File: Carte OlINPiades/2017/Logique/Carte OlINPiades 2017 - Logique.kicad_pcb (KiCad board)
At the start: 2 copper layers, 258 parts

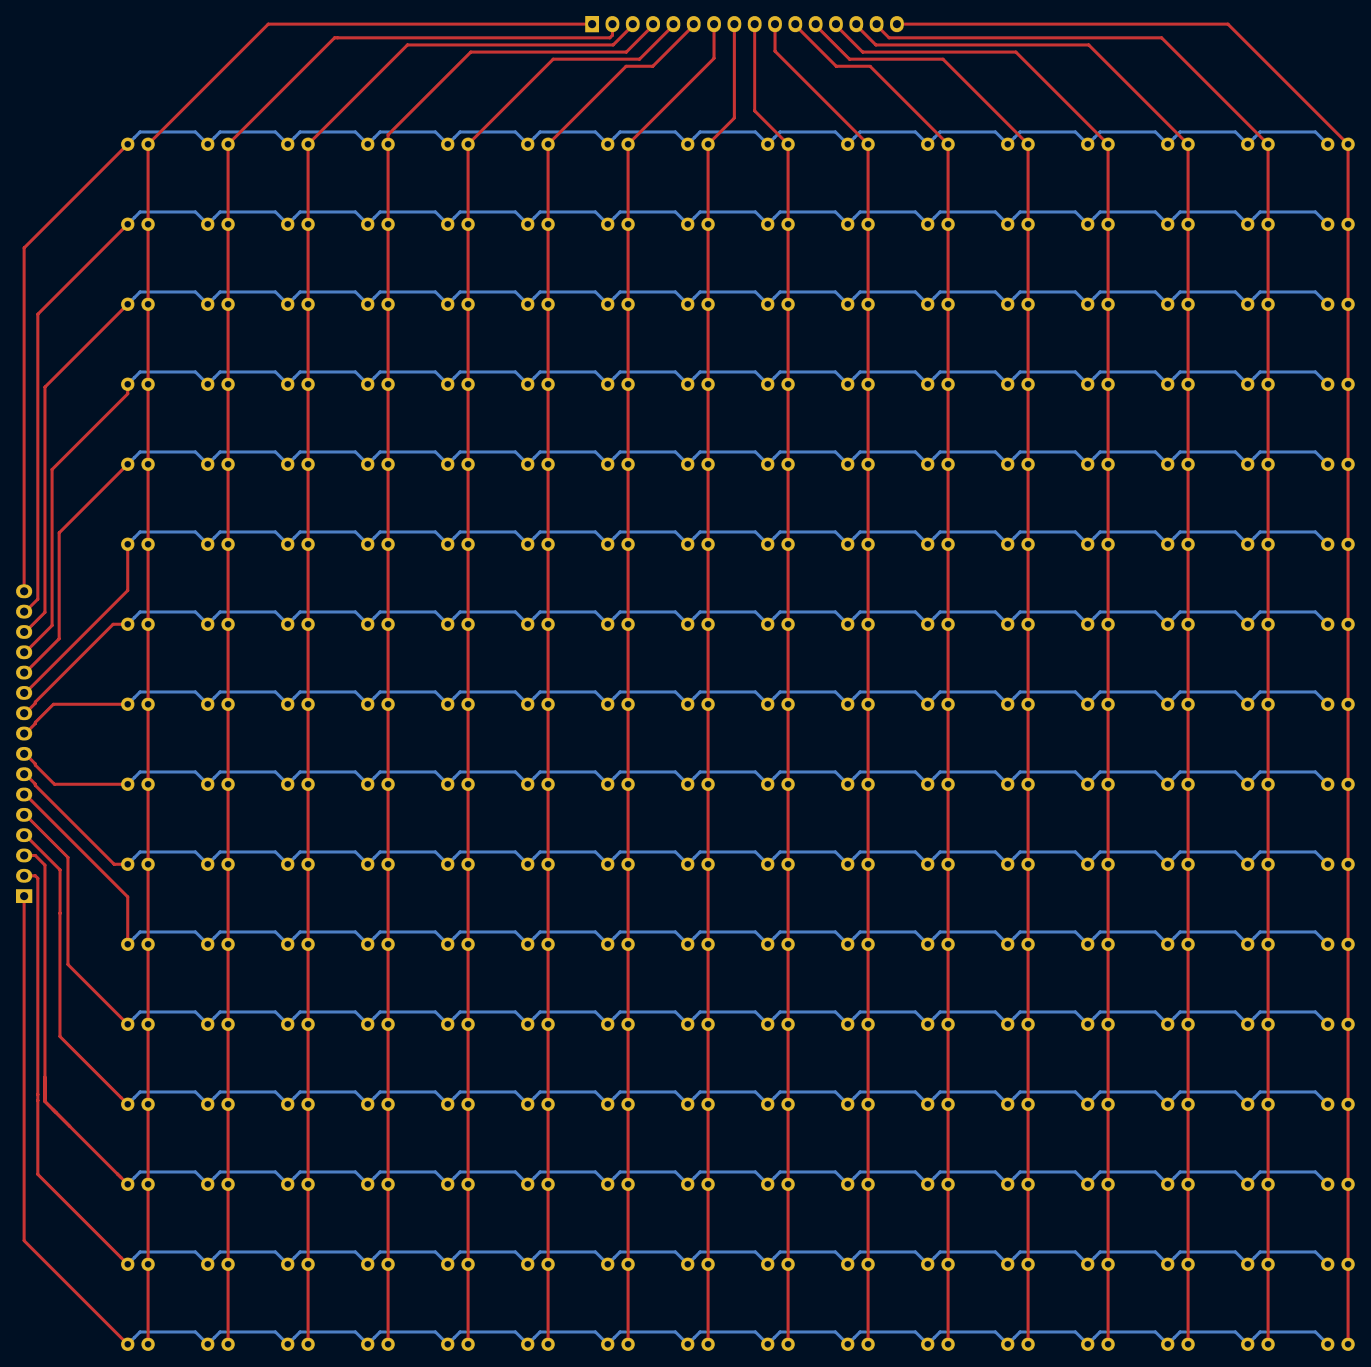
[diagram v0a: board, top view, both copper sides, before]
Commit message: Routage carte Logique fini, à vérifier
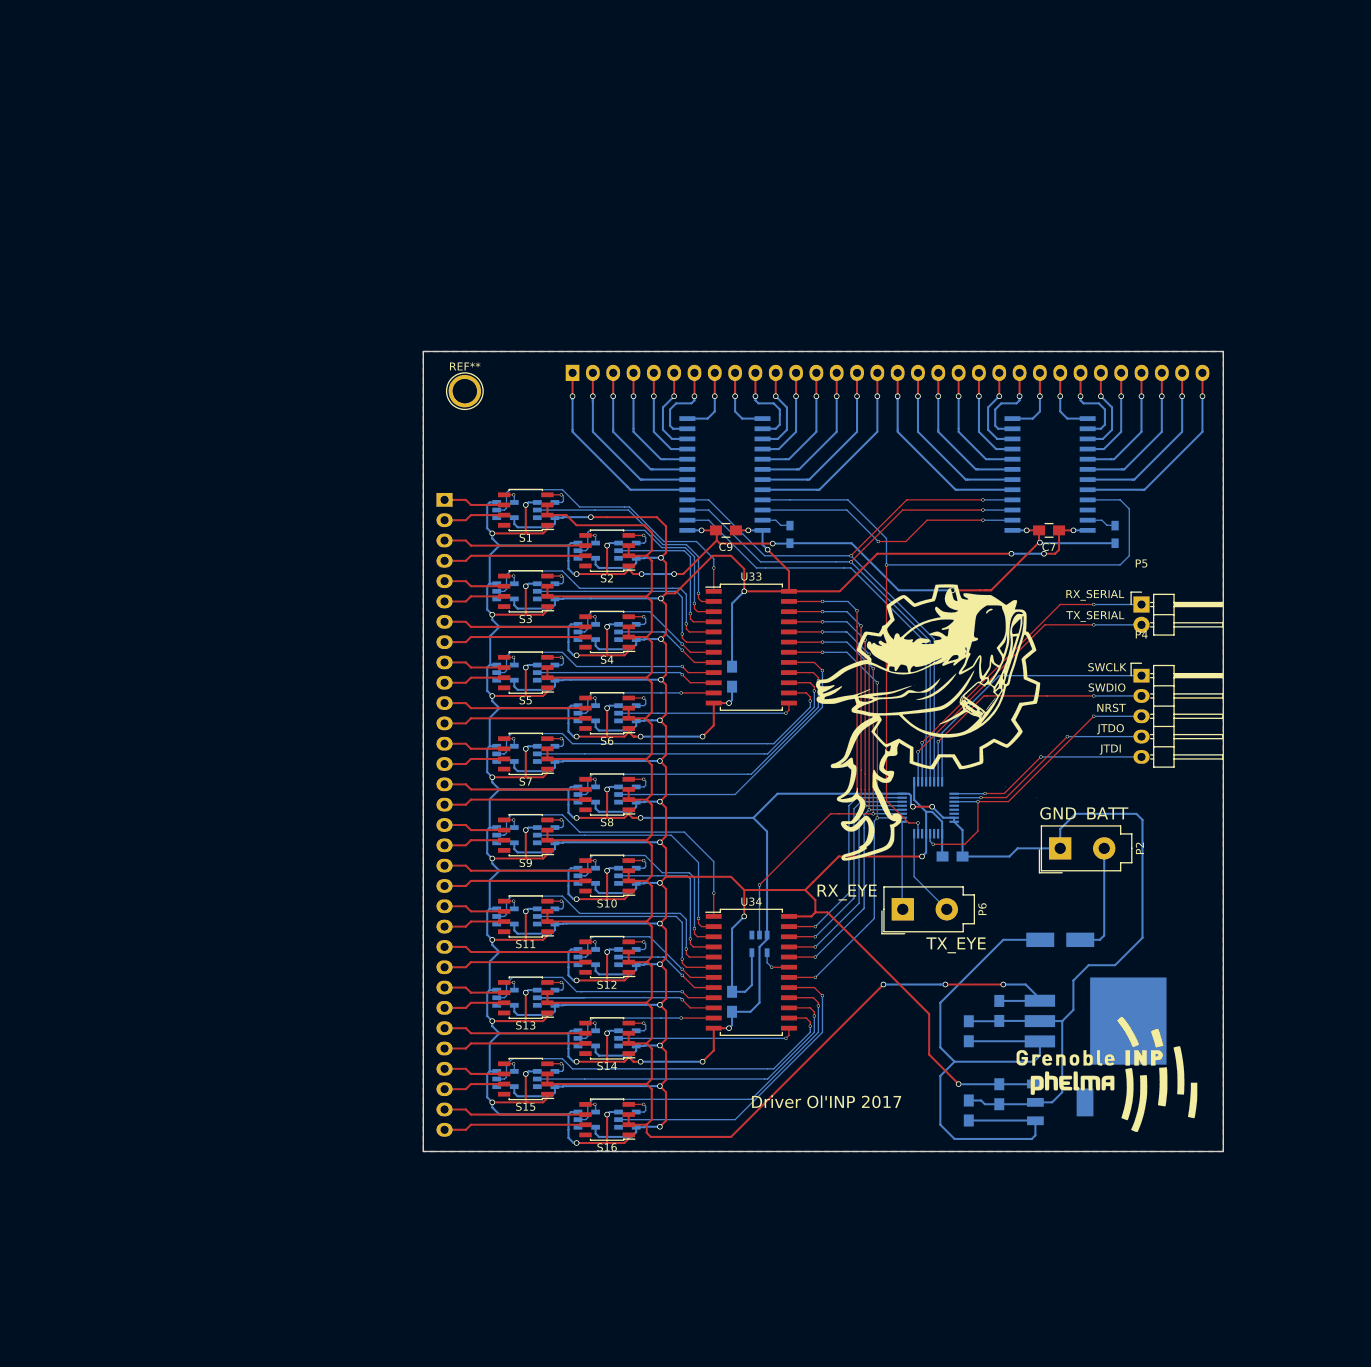
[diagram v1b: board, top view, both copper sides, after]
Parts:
- removed D10, D100, D101, D102, D103, D104, D105, D106, D107, D108, D109, D11, D110, D111, D112, D113, D114, D115, D116, D117, D118, D119, D12, D120, D121, D122, D123, D124, D125, D126, D127, D128, D129, D13, D130, D131, D132, D133, D134, D135, D136, D137, D138, D139, D14, D140, D141, D142, D143, D144, D145, D146, D147, D148, D149, D15, D150, D151, D152, D153, D154, D155, D156, D157, D158, D159, D16, D160, D161, D162, D163, D164, D165, D166, D167, D168, D169, D17, D170, D171, D172, D173, D174, D175, D176, D177, D178, D179, D18, D180, D181, D182, D183, D184, D185, D186, D187, D188, D189, D19, D190, D191, D192, D193, D194, D195, D196, D197, D198, D199, D2, D20, D200, D201, D202, D203, D204, D205, D206, D207, D208, D209, D21, D210, D211, D212, D213, D214, D215, D216, D217, D218, D219, D22, D220, D221, D222, D223, D224, D225, D226, D227, D228, D229, D23, D230, D231, D232, D233, D234, D235, D236, D237, D238, D239, D24, D240, D241, D242, D243, D244, D245, D246, D247, D248, D249, D25, D250, D251, D252, D253, D254, D255, D256, D26, D27, D28, D29, D3, D30, D31, D32, D33, D34, D35, D36, D37, D38, D39, D4, D40, D41, D42, D43, D44, D45, D46, D47, D48, D49, D5, D50, D51, D52, D53, D54, D55, D56, D57, D58, D59, D6, D60, D61, D62, D63, D64, D65, D66, D67, D68, D69, D7, D70, D71, D72, D73, D74, D75, D76, D77, D78, D79, D8, D80, D81, D82, D83, D84, D85, D86, D87, D88, D89, D9, D90, D91, D92, D93, D94, D95, D96, D97, D98, D99: LED, LEDs:LED-3MM
- removed H1, H2: PinHeader, Pin_Headers:Pin_Header_Straight_1x16
- added C1: 100nF, Capacitors_SMD:C_0805_HandSoldering, B.Cu at (140.6, 96.6)
- added C2: 100nF, Capacitors_SMD:C_0805_HandSoldering, B.Cu at (140.6, 137.3)
- added C3: 150nF, Capacitors_SMD:C_0805_HandSoldering, B.Cu at (170.2, 141.0)
- added C4: 100nF, Capacitors_SMD:C_0805_HandSoldering, B.Cu at (174.0, 138.4)
- added C5: 150nF, Capacitors_SMD:C_0805_HandSoldering, B.Cu at (170.2, 150.9)
- added C6: 100nF, Capacitors_SMD:C_0805_HandSoldering, B.Cu at (174.0, 148.8)
- added C7: 100nF, Capacitors_SMD:C_0805_HandSoldering, F.Cu at (180.2, 78.4)
- added C8: 100nF, Capacitors_SMD:C_0805_HandSoldering, B.Cu at (168.1, 119.1)
- added C9: 100nF, Capacitors_SMD:C_0805_HandSoldering, F.Cu at (139.8, 78.4)
- added G***: LOGO, drawings:robotronik_logo, F.Cu at (166.5, 102.5)
- added G***: LOGO, drawings:phelma_logo, F.Cu at (187.5, 146.3)
- added P1: CONN_01X32, Pin_Headers:Pin_Header_Straight_1x32, B.Cu at (104.6, 74.5)
- added P2: CONN_01X02, Connectors_Molex_Complete:Molex_MiniFit-JR-5556-02A_2x01x4.20mm_Straight, F.Cu at (181.6, 118.1)
- added P3: CONN_01X32, Pin_Headers:Pin_Header_Straight_1x32, B.Cu at (120.7, 58.7)
- added P4: CONN_01X05, Pin_Headers:Pin_Header_Angled_1x05, F.Cu at (191.8, 96.5)
- added P5: CONN_01X02, Pin_Headers:Pin_Header_Angled_1x02, F.Cu at (191.8, 87.6)
- added P6: CONN_01X02, Connectors_Molex_Complete:Molex_MiniFit-JR-5556-02A_2x01x4.20mm_Straight, F.Cu at (161.9, 125.7)
- added R1: R, Resistors_SMD:R_0603_HandSoldering, B.Cu at (147.8, 78.9)
- added R2: R, Resistors_SMD:R_0603_HandSoldering, B.Cu at (188.5, 78.9)
- added REF**: 1pin, Connect:1pin, F.Cu at (107.2, 61.0)
- added S1: TPS2080, Housings_SOIC:SOIC-8_3.9x4.9mm_Pitch1.27mm, F.Cu at (114.8, 75.8)
- added S10: TPS2080, Housings_SOIC:SOIC-8_3.9x4.9mm_Pitch1.27mm, F.Cu at (125.0, 121.5)
- added S11: TPS2080, Housings_SOIC:SOIC-8_3.9x4.9mm_Pitch1.27mm, F.Cu at (114.8, 126.6)
- added S12: TPS2080, Housings_SOIC:SOIC-8_3.9x4.9mm_Pitch1.27mm, F.Cu at (125.0, 131.7)
- added S13: TPS2080, Housings_SOIC:SOIC-8_3.9x4.9mm_Pitch1.27mm, F.Cu at (114.8, 136.8)
- added S14: TPS2080, Housings_SOIC:SOIC-8_3.9x4.9mm_Pitch1.27mm, F.Cu at (125.0, 141.9)
- added S15: TPS2080, Housings_SOIC:SOIC-8_3.9x4.9mm_Pitch1.27mm, F.Cu at (114.8, 146.9)
- added S16: TPS2080, Housings_SOIC:SOIC-8_3.9x4.9mm_Pitch1.27mm, F.Cu at (125.0, 152.0)
- added S17: CAT4016, Housings_SOIC:SOIC-24_7.5x15.4mm_Pitch1.27mm, B.Cu at (139.7, 71.4)
- added S18: CAT4016, Housings_SOIC:SOIC-24_7.5x15.4mm_Pitch1.27mm, B.Cu at (180.3, 71.4)
- added S2: TPS2080, Housings_SOIC:SOIC-8_3.9x4.9mm_Pitch1.27mm, F.Cu at (125.0, 80.9)
- added S3: TPS2080, Housings_SOIC:SOIC-8_3.9x4.9mm_Pitch1.27mm, F.Cu at (114.8, 86.0)
- added S4: TPS2080, Housings_SOIC:SOIC-8_3.9x4.9mm_Pitch1.27mm, F.Cu at (125.0, 91.1)
- added S5: TPS2080, Housings_SOIC:SOIC-8_3.9x4.9mm_Pitch1.27mm, F.Cu at (114.8, 96.1)
- added S6: TPS2080, Housings_SOIC:SOIC-8_3.9x4.9mm_Pitch1.27mm, F.Cu at (125.0, 101.2)
- added S7: TPS2080, Housings_SOIC:SOIC-8_3.9x4.9mm_Pitch1.27mm, F.Cu at (114.8, 106.3)
- added S8: TPS2080, Housings_SOIC:SOIC-8_3.9x4.9mm_Pitch1.27mm, F.Cu at (125.0, 111.4)
- added S9: TPS2080, Housings_SOIC:SOIC-8_3.9x4.9mm_Pitch1.27mm, F.Cu at (114.8, 116.5)
- added U1: 74AHC1G, misc:SOT-23-5, B.Cu at (117.3, 75.8)
- added U10: 74AHC1G, misc:SOT-23-5, B.Cu at (127.5, 121.5)
- added U11: 74AHC1G, misc:SOT-23-5, B.Cu at (117.3, 126.6)
- added U12: 74AHC1G, misc:SOT-23-5, B.Cu at (127.5, 131.7)
- added U13: 74AHC1G, misc:SOT-23-5, B.Cu at (117.3, 136.8)
- added U14: 74AHC1G, misc:SOT-23-5, B.Cu at (127.5, 141.9)
- added U15: 74AHC1G, misc:SOT-23-5, B.Cu at (117.3, 146.9)
- added U16: 74AHC1G, misc:SOT-23-5, B.Cu at (127.5, 152.0)
- added U17: 74AHC1G, misc:SOT-23-5, B.Cu at (112.3, 75.8)
- added U18: 74AHC1G, misc:SOT-23-5, B.Cu at (122.4, 80.9)
- added U19: 74AHC1G, misc:SOT-23-5, B.Cu at (112.3, 86.0)
- added U2: 74AHC1G, misc:SOT-23-5, B.Cu at (127.5, 80.9)
- added U20: 74AHC1G, misc:SOT-23-5, B.Cu at (122.4, 91.1)
- added U21: 74AHC1G, misc:SOT-23-5, B.Cu at (112.3, 96.1)
- added U22: 74AHC1G, misc:SOT-23-5, B.Cu at (122.4, 101.2)
- added U23: 74AHC1G, misc:SOT-23-5, B.Cu at (112.3, 106.3)
- added U24: 74AHC1G, misc:SOT-23-5, B.Cu at (122.4, 111.4)
- added U25: 74AHC1G, misc:SOT-23-5, B.Cu at (112.3, 116.5)
- added U26: 74AHC1G, misc:SOT-23-5, B.Cu at (122.4, 121.5)
- added U27: 74AHC1G, misc:SOT-23-5, B.Cu at (112.3, 126.6)
- added U28: 74AHC1G, misc:SOT-23-5, B.Cu at (122.4, 131.7)
- added U29: 74AHC1G, misc:SOT-23-5, B.Cu at (112.3, 136.8)
- added U3: 74AHC1G, misc:SOT-23-5, B.Cu at (117.3, 86.0)
- added U30: 74AHC1G, misc:SOT-23-5, B.Cu at (122.4, 141.9)
- added U31: 74AHC1G, misc:SOT-23-5, B.Cu at (112.3, 146.9)
- added U32: 74AHC1G, misc:SOT-23-5, B.Cu at (122.4, 152.0)
- added U33: CD74HC154, Housings_SOIC:SOIC-24_7.5x15.4mm_Pitch1.27mm, F.Cu at (143.0, 93.0)
- added U34: CD74HC154, Housings_SOIC:SOIC-24_7.5x15.4mm_Pitch1.27mm, F.Cu at (143.0, 133.6)
- added U35: LM340SX, misc:TO-263-4, B.Cu at (185.4, 139.7)
- added U36: 74AHC1G, misc:SOT-23-5, B.Cu at (144.0, 130.0)
- added U37: UA78M33, misc:SOT-223, B.Cu at (181.6, 149.9)
- added U38: STM32F303K8, Housings_QFP:LQFP-32_5x5mm_Pitch0.5mm, B.Cu at (165.1, 113.0)
- added U4: 74AHC1G, misc:SOT-23-5, B.Cu at (127.5, 91.1)
- added U5: 74AHC1G, misc:SOT-23-5, B.Cu at (117.3, 96.1)
- added U6: 74AHC1G, misc:SOT-23-5, B.Cu at (127.5, 101.2)
- added U7: 74AHC1G, misc:SOT-23-5, B.Cu at (117.3, 106.3)
- added U8: 74AHC1G, misc:SOT-23-5, B.Cu at (127.5, 111.4)
- added U9: 74AHC1G, misc:SOT-23-5, B.Cu at (117.3, 116.5)
- D1: value LED -> RFN2L4STE25; footprint LEDs:LED-3MM -> Diodes_SMD:SMA_Handsoldering
- moved D1 105.3 mm to (181.6, 129.5)
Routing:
- net GND: track 0.00 -> 690.1 mm, vias 0 -> 48
- net +3V3: track 0.00 -> 528.7 mm, vias 0 -> 25
- net +5V: track 0.00 -> 285.3 mm, vias 0 -> 3
- net Net-(D241-Pad1): track 234.2 -> 0.00 mm
- net Net-(D209-Pad1): track 231.4 -> 0.00 mm
- net Net-(D225-Pad1): track 228.2 -> 0.00 mm
- net Net-(D17-Pad1): track 226.7 -> 0.00 mm
- net Net-(D33-Pad1): track 219.2 -> 0.00 mm
- net Net-(D193-Pad1): track 212.2 -> 0.00 mm
- net Net-(D49-Pad1): track 211.8 -> 0.00 mm
- net Net-(D112-Pad2): track 211.7 -> 0.00 mm
- net Net-(D114-Pad2): track 205.2 -> 0.00 mm
- net Net-(D111-Pad2): track 205.1 -> 0.00 mm
- net Net-(D177-Pad1): track 204.6 -> 0.00 mm
- net Net-(D65-Pad1): track 204.3 -> 0.00 mm
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- added copper zone on B.Cu, net GND
- added copper zone on F.Cu, net GND
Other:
- board outline added: 100 x 100 mm
- net class Power_SeedStudio added: clearance 0.1524, trace_width 0.254, via_dia 0.7, via_drill 0.5
- net class SeedStudio added: clearance 0.1524, trace_width 0.1524, via_dia 0.4, via_drill 0.3
- rule trace_min: 0.308 -> 0.15
- board text added: "BATT"
- board text added: "Driver Ol'INP 2017"
- board text added: "GND"
- board text added: "JTDI"
- board text added: "JTDO"
- board text added: "NRST"
- board text added: "RX_EYE"
- board text added: "RX_SERIAL"
- board text added: "SWCLK"
- board text added: "SWDIO"
- board text added: "TX_EYE"
- board text added: "TX_SERIAL"

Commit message: Correction du sens des connecteurs
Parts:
- C7, C9: moved to B.Cu
- R1, S17, S18: moved to F.Cu
- moved P3 78.7 mm to (199.4, 58.7), turned to 90 degrees
- moved R2 48.3 mm to (140.2, 77.0), turned to 180 degrees
- moved S18 40.6 mm to (139.7, 71.2), turned to 180 degrees
- moved S17 40.6 mm to (180.3, 71.4), turned to 180 degrees
- moved R1 24.4 mm to (172.2, 78.4)
- moved C7 1.42 mm to (180.8, 79.6), turned to 0 degrees
- moved C9 1.20 mm to (140.2, 79.5), turned to 0 degrees
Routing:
- net GND: track 690.1 -> 717.8 mm, vias 48 -> 44
- net +3V3: track 528.7 -> 518.2 mm, vias 25 -> 22
- net SERIAL_IN: track 53.5 -> 51.0 mm, vias 0 -> 1
- net LATCH_COL: track 79.0 -> 77.1 mm
- net CLK_COL: track 77.6 -> 75.7 mm
- net Net-(P3-Pad23): track 11.3 -> 10.3 mm, vias 1 -> 0
- net Net-(P3-Pad7): track 11.3 -> 10.3 mm, vias 1 -> 0
- net Net-(P3-Pad26): track 11.2 -> 10.3 mm, vias 1 -> 0
- net Net-(P3-Pad10): track 11.2 -> 10.3 mm, vias 1 -> 0
- net Net-(P3-Pad2): track 22.3 -> 21.4 mm, vias 1 -> 0
- net Net-(P3-Pad18): track 22.3 -> 21.4 mm, vias 1 -> 0
- net Net-(S17-Pad22): track 34.0 -> 34.7 mm
- net Net-(U17-Pad2): track 36.9 -> 36.3 mm
- net Net-(P3-Pad19): track 18.8 -> 18.4 mm, vias 1 -> 0
- net Net-(P3-Pad5): track 12.7 -> 12.2 mm, vias 1 -> 0
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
